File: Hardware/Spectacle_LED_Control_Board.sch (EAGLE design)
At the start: 44 parts, among them J3 USB-MICROB, J4 AUDIO-JACK3, J8 AUDIO-JACK3, U1 CY8C4146LQI-S422, U2 3.3V/150mA, U4 SN74LVC1G66, U5 SN74LVC1G66

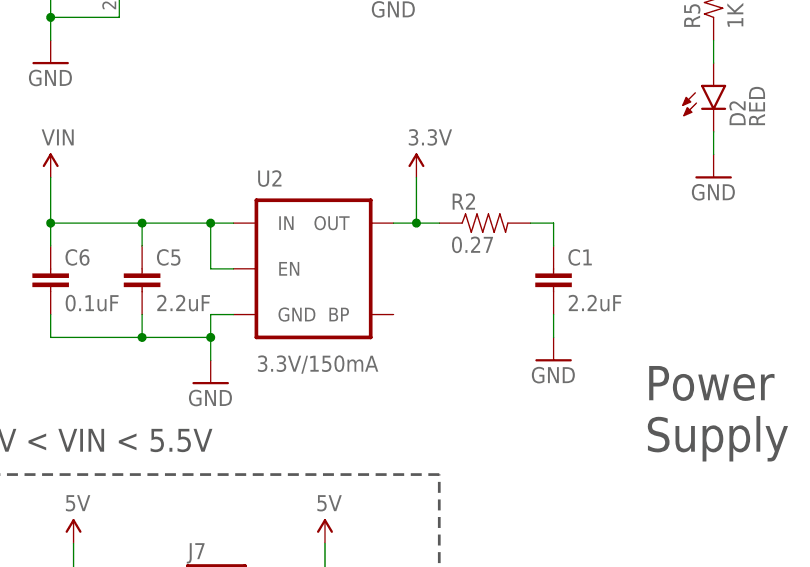
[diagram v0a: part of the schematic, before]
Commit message: Chg VREG to APK2112
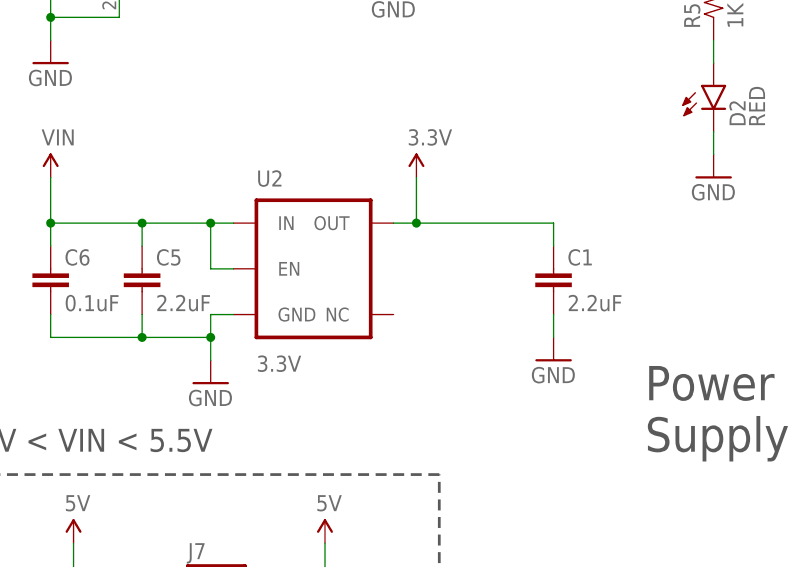
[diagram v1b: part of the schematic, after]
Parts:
- removed R2: 0.27, SparkFun-Resistors:0.27OHM-1/10W-1%(0603)
- U2: value 3.3V/150mA -> 3.3V; device SparkFun-PowerIC:V_REG_MIC52053.3V -> SparkFun-PowerIC:V_REG_AP2112K-3.3V
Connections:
- removed net N$3: C1.1, R2.2
- net 3.3V: now also C1.1; no longer R2.1
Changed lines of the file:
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@@
 <part name="GND1" library="SparkFun-Aesthetics" deviceset="GND" device=""/>
 <part name="SUPPLY2" library="SparkFun-Aesthetics" deviceset="VIN" device=""/>
-<part name="U2" library="SparkFun-PowerIC" deviceset="V_REG_MIC5205" device="3.3V" value="3.3V/150mA"/>
+<part name="U2" library="SparkFun-PowerIC" deviceset="V_REG_AP2112" device="K-3.3V" value="3.3V"/>
 <part name="GND6" library="SparkFun-Aesthetics" deviceset="GND" device=""/>
 <part name="SUPPLY3" library="SparkFun-Aesthetics" deviceset="VCC" device=""/>
 <part name="R1" library="SparkFun-Resistors" deviceset="10KOHM-1/10W-1%(0603)" device="0603" value="10K"/>
 <part name="GND7" library="SparkFun-Aesthetics" deviceset="GND" device=""/>
-<part name="R2" library="SparkFun-Resistors" deviceset="0.27OHM-1/10W-1%(0603)" device="" value="0.27"/>
 <part name="C1" library="SparkFun-Capacitors" deviceset="2.2UF-10V-20%(0603)" device="" value="2.2uF"/>
 <part name="C2" library="SparkFun-Capacitors" deviceset="1.0UF-16V-10%(0402)" device="" value="1.0uF"/>
@@
 <instance part="GND1" gate="1" x="33.02" y="96.52"/>
 <instance part="SUPPLY2" gate="G$1" x="15.24" y="119.38"/>
-<instance part="U2" gate="U1" x="45.72" y="109.22"/>
+<instance part="U2" gate="G$1" x="45.72" y="109.22"/>
 <instance part="GND6" gate="1" x="15.24" y="132.08"/>
 <instance part="SUPPLY3" gate="G$1" x="17.78" y="175.26"/>
 <instance part="R1" gate="G$1" x="35.56" y="165.1" rot="R90"/>
 <instance part="GND7" gate="1" x="71.12" y="99.06"/>
-<instance part="R2" gate="G$1" x="63.5" y="114.3"/>
 <instance part="C1" gate="G$1" x="71.12" y="106.68"/>
 <instance part="C2" gate="G$1" x="71.12" y="167.64"/>
@@
 </segment>
 <segment>
-<pinref part="U2" gate="U1" pin="GND"/>
+<pinref part="U2" gate="G$1" pin="GND"/>
 <pinref part="GND1" gate="1" pin="GND"/>
 <wire x1="35.56" y1="104.14" x2="33.02" y2="104.14" width="0.1524" layer="91"/>
@@
 </segment>
 </net>
-<net name="N$3" class="0">
-<segment>
-<pinref part="R2" gate="G$1" pin="2"/>
-<wire x1="68.58" y1="114.3" x2="71.12" y2="114.3" width="0.1524" layer="91"/>
-<pinref part="C1" gate="G$1" pin="1"/>
-<wire x1="71.12" y1="114.3" x2="71.12" y2="111.76" width="0.1524" layer="91"/>
-</segment>
-</net>
 <net name="VIN" class="0">
 <segment>
-<pinref part="U2" gate="U1" pin="EN"/>
+<pinref part="U2" gate="G$1" pin="EN"/>
 <wire x1="35.56" y1="109.22" x2="33.02" y2="109.22" width="0.1524" layer="91"/>
 <wire x1="33.02" y1="109.22" x2="33.02" y2="114.3" width="0.1524" layer="91"/>
-<pinref part="U2" gate="U1" pin="IN"/>
+<pinref part="U2" gate="G$1" pin="IN"/>
 <wire x1="35.56" y1="114.3" x2="33.02" y2="114.3" width="0.1524" layer="91"/>
 <junction x="33.02" y="114.3"/>
@@
 </segment>
 <segment>
-<pinref part="U2" gate="U1" pin="OUT"/>
+<pinref part="U2" gate="G$1" pin="OUT"/>
 <wire x1="53.34" y1="114.3" x2="55.88" y2="114.3" width="0.1524" layer="91"/>
 <wire x1="55.88" y1="114.3" x2="55.88" y2="119.38" width="0.1524" layer="91"/>
-<pinref part="R2" gate="G$1" pin="1"/>
-<wire x1="55.88" y1="114.3" x2="58.42" y2="114.3" width="0.1524" layer="91"/>
 <junction x="55.88" y="114.3"/>
 <pinref part="SUPPLY9" gate="G$1" pin="3.3V"/>
-</segment>
-<segment>
+<pinref part="C1" gate="G$1" pin="1"/>
+<wire x1="71.12" y1="114.3" x2="71.12" y2="111.76" width="0.1524" layer="91"/>
+<wire x1="55.88" y1="114.3" x2="71.12" y2="114.3" width="0.1524" layer="91"/>
+</segment>
+<segment>

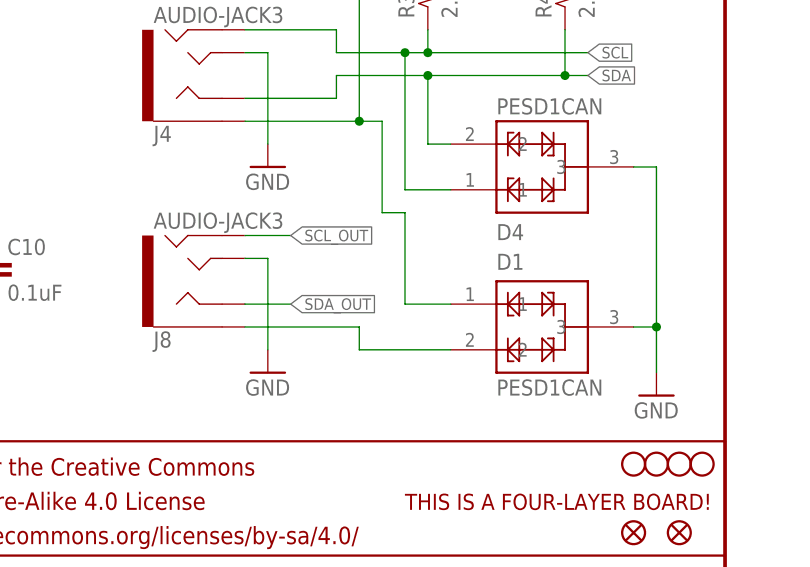
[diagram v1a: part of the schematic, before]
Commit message: Fix VIN path per review
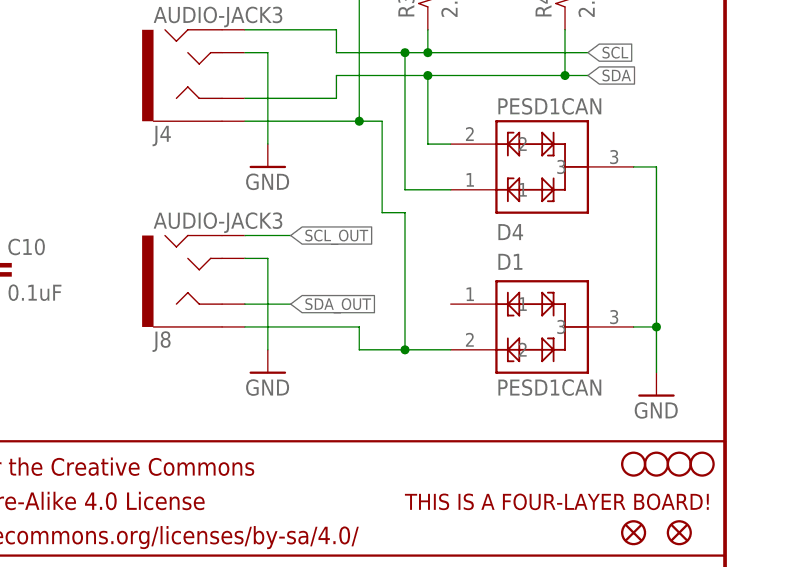
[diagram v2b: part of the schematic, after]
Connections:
- removed net N$1: D1.2, J8.EARTH
- net VIN: now also D1.2, J8.EARTH; no longer D1.1
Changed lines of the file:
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@@
 <wire x1="205.74" y1="91.44" x2="208.28" y2="91.44" width="0.1524" layer="91"/>
 <junction x="208.28" y="91.44"/>
-<pinref part="D1" gate="G$1" pin="1"/>
-<wire x1="218.44" y1="50.8" x2="213.36" y2="50.8" width="0.1524" layer="91"/>
-<wire x1="213.36" y1="50.8" x2="213.36" y2="60.96" width="0.1524" layer="91"/>
 <wire x1="213.36" y1="60.96" x2="210.82" y2="60.96" width="0.1524" layer="91"/>
 <wire x1="210.82" y1="60.96" x2="210.82" y2="71.12" width="0.1524" layer="91"/>
 <wire x1="210.82" y1="71.12" x2="208.28" y2="71.12" width="0.1524" layer="91"/>
 <junction x="208.28" y="71.12"/>
+<pinref part="D1" gate="G$1" pin="2"/>
+<pinref part="J8" gate="G$1" pin="EARTH"/>
+<wire x1="195.58" y1="48.26" x2="208.28" y2="48.26" width="0.1524" layer="91"/>
+<wire x1="208.28" y1="45.72" x2="208.28" y2="48.26" width="0.1524" layer="91"/>
+<wire x1="208.28" y1="45.72" x2="213.36" y2="45.72" width="0.1524" layer="91"/>
+<wire x1="213.36" y1="45.72" x2="218.44" y2="45.72" width="0.1524" layer="91"/>
+<wire x1="213.36" y1="60.96" x2="213.36" y2="45.72" width="0.1524" layer="91"/>
+<junction x="213.36" y="45.72"/>
 </segment>
 <segment>
@@
 </segment>
 </net>
-<net name="N$1" class="0">
-<segment>
-<pinref part="D1" gate="G$1" pin="2"/>
-<pinref part="J8" gate="G$1" pin="EARTH"/>
-<wire x1="195.58" y1="48.26" x2="208.28" y2="48.26" width="0.1524" layer="91"/>
-<wire x1="208.28" y1="45.72" x2="208.28" y2="48.26" width="0.1524" layer="91"/>
-<wire x1="208.28" y1="45.72" x2="218.44" y2="45.72" width="0.1524" layer="91"/>
-</segment>
-</net>

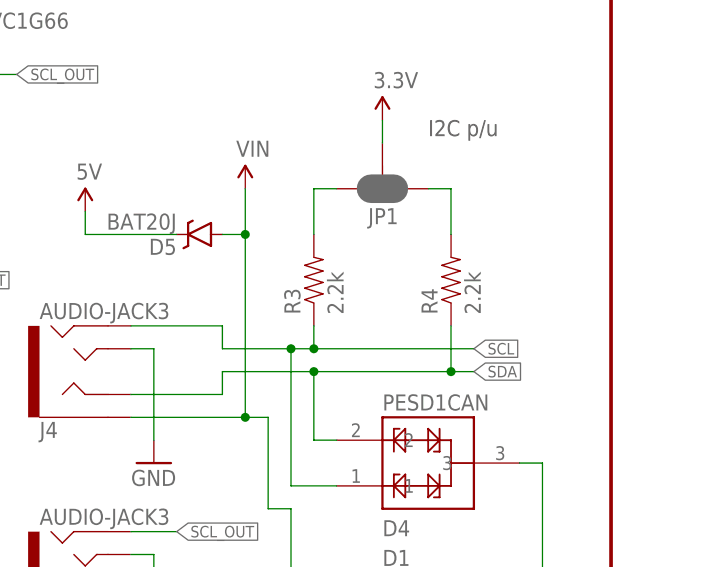
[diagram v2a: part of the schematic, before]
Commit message: Change pullups to 4.7k
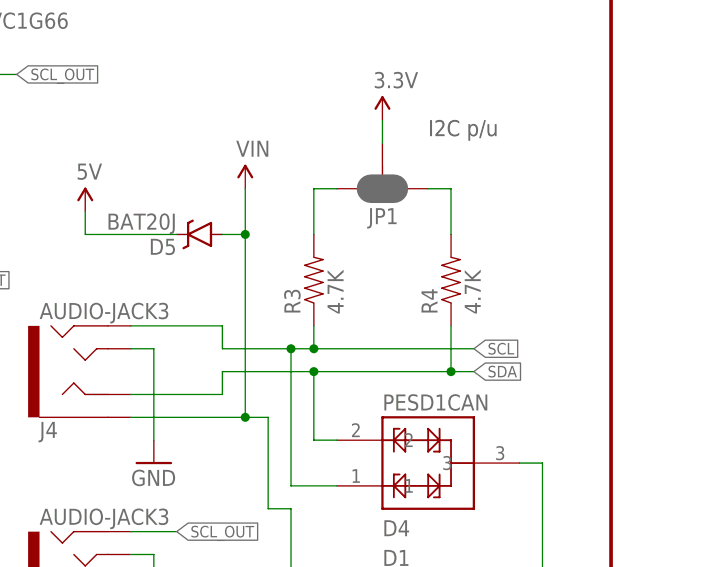
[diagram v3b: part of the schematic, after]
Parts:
- R3, R4: value 2.2k -> 4.7K; device SparkFun-Resistors:2.2KOHM-1/10W-1%(0603) -> SparkFun-Resistors:4.7KOHM-1/10W-1%(0603)
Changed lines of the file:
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@@
 <part name="GND9" library="SparkFun-Aesthetics" deviceset="GND" device=""/>
 <part name="SUPPLY7" library="SparkFun-Aesthetics" deviceset="VIN" device=""/>
-<part name="R3" library="SparkFun-Resistors" deviceset="2.2KOHM-1/10W-1%(0603)" device="" value="2.2k"/>
-<part name="R4" library="SparkFun-Resistors" deviceset="2.2KOHM-1/10W-1%(0603)" device="" value="2.2k"/>
+<part name="R3" library="SparkFun-Resistors" deviceset="4.7KOHM-1/10W-1%(0603)" device="" value="4.7K"/>
+<part name="R4" library="SparkFun-Resistors" deviceset="4.7KOHM-1/10W-1%(0603)" device="" value="4.7K"/>
 <part name="JP1" library="SparkFun-Passives" deviceset="JUMPER-PAD-3-NC_BY_PASTE" device=""/>
 <part name="J2" library="SparkFun-Connectors" deviceset="M05" device="NO_SILK"/>

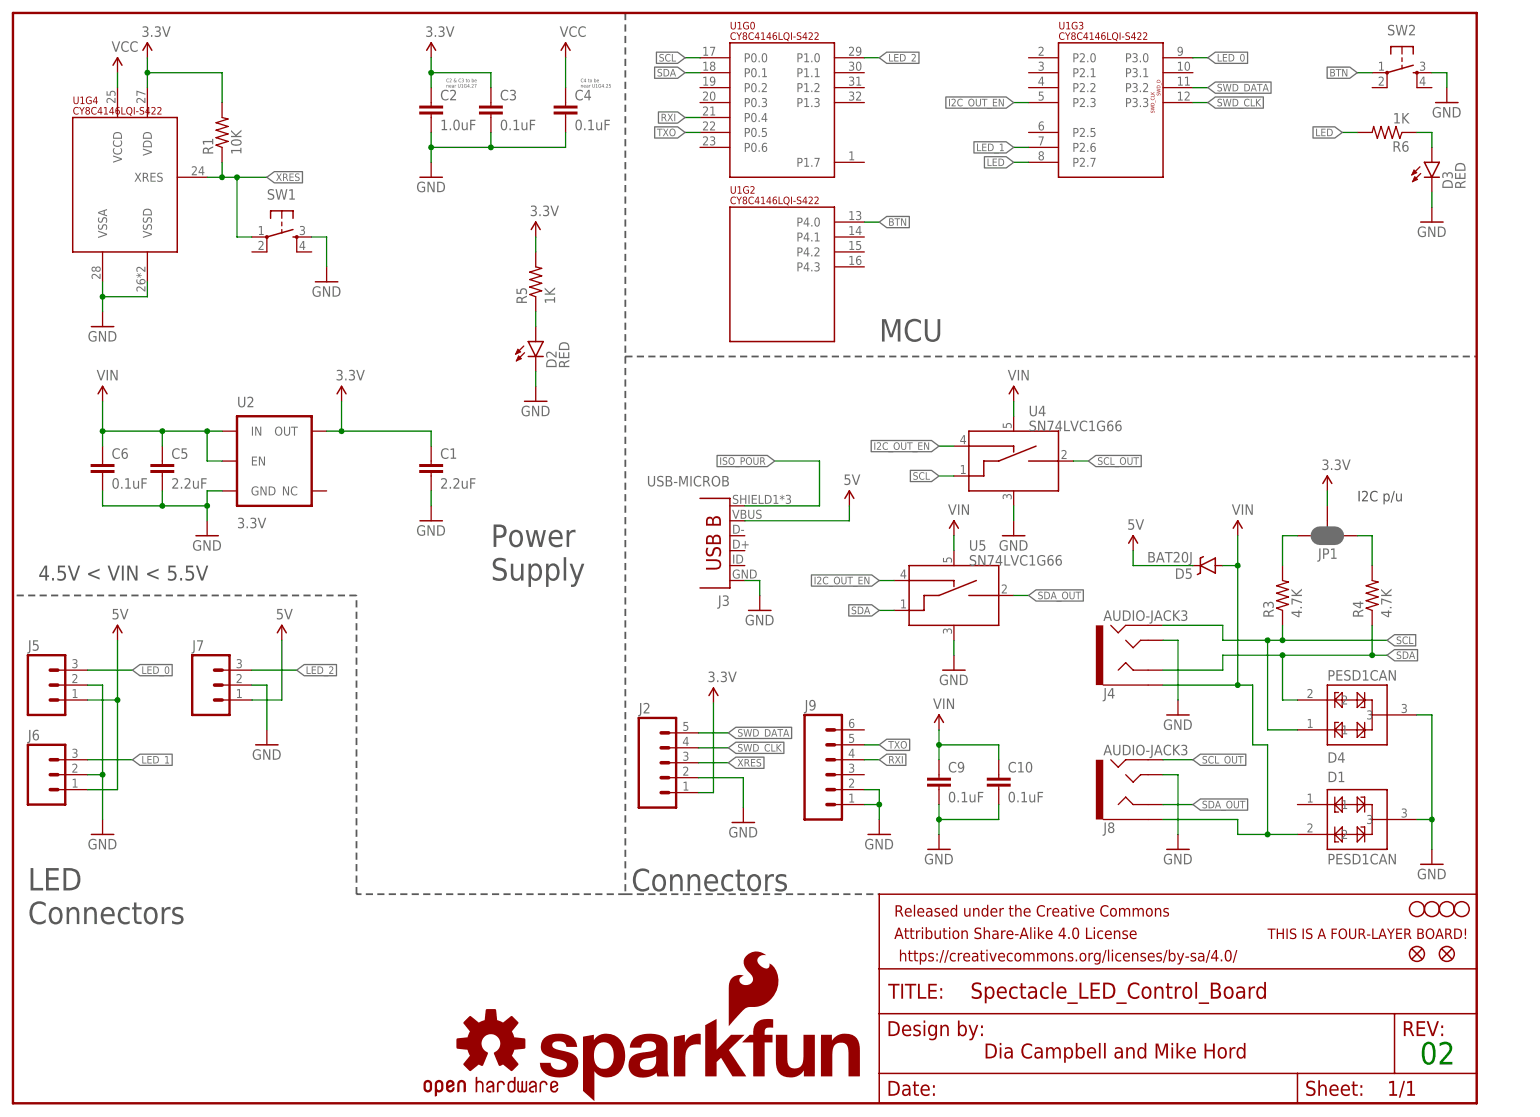
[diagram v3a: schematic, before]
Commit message: Primarily for changing to PSOC4245LQI-483 Interstitial commit for firmware
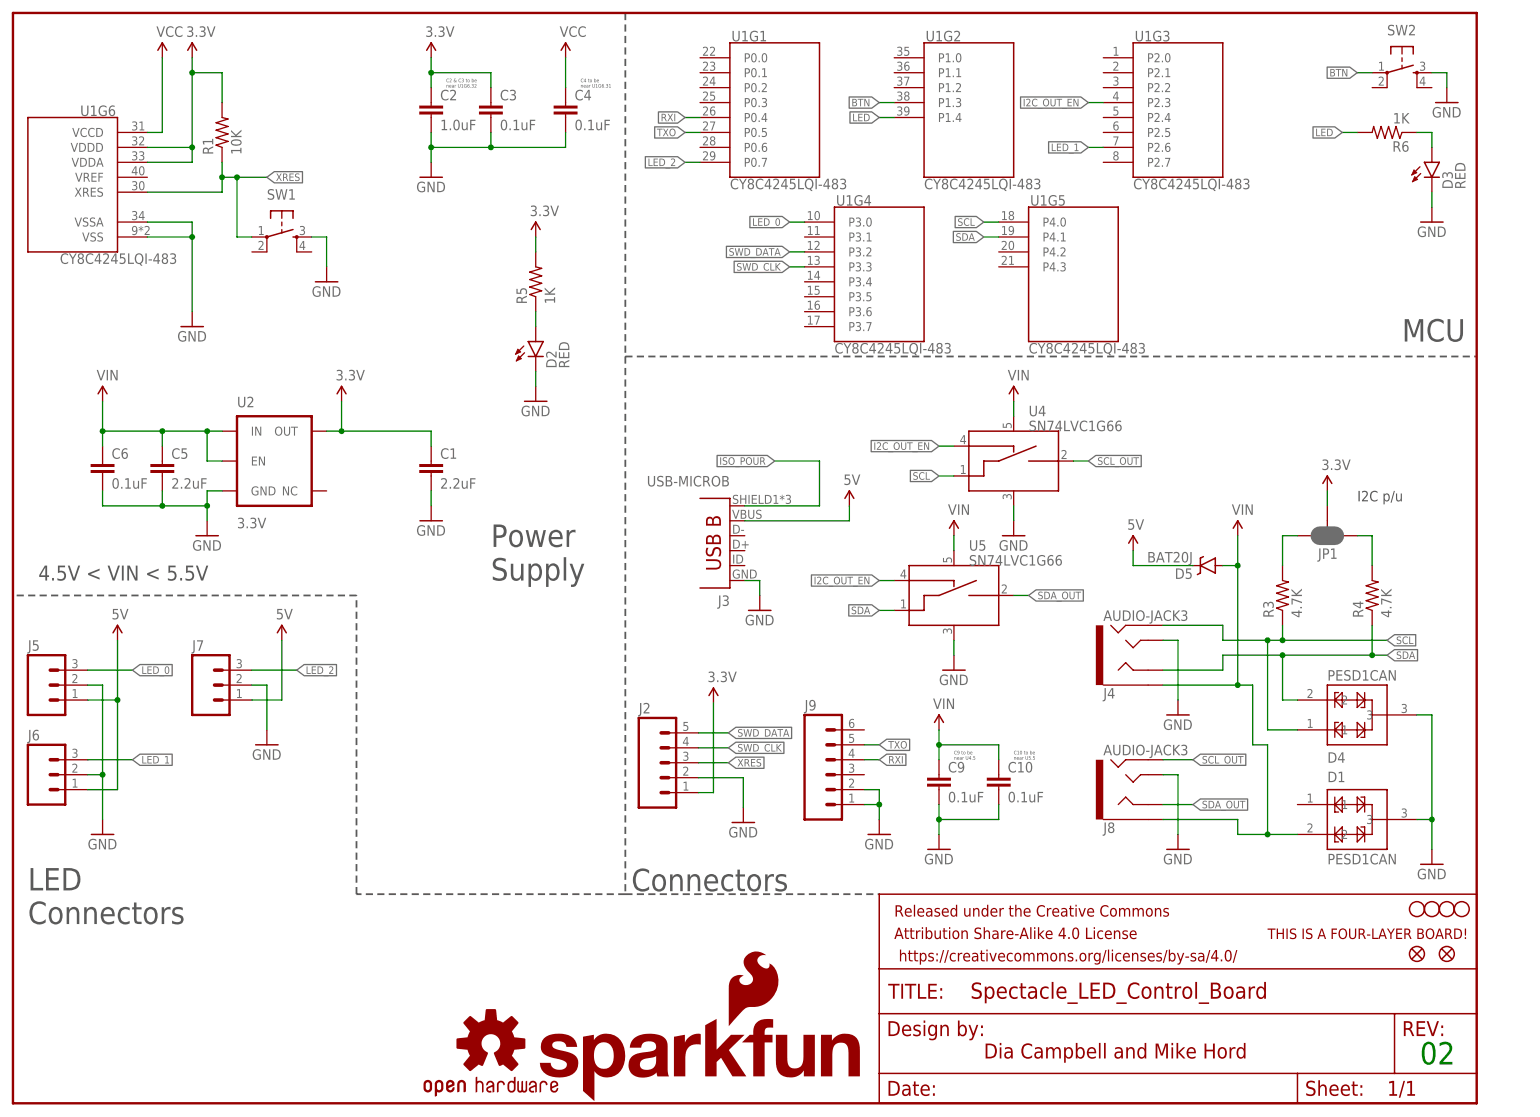
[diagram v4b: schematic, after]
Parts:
- U1: value CY8C4146LQI-S422 -> CY8C4245LQI-483; device SparkFun-DigitalIC:PSOC4_4100S_32QFN -> SparkFun-IC-Microcontroller:PSOC4_4200_40QFN
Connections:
- net 3.3V: now also U1G6.VDDA, U1G6.VDDD; no longer U1G4.VDD
- net BTN: now also U1G2.P1.3; no longer U1G2.P4.0
- net GND: now also U1G6.VSS, U1G6.VSSA; no longer U1G4.VSSA, U1G4.VSSD
- net LED: now also U1G2.P1.4; no longer U1G3.P2.7
- net LED_0: now also U1G4.P3.0; no longer U1G3.P3.0
- net LED_2: now also U1G1.P0.7; no longer U1G0.P1.0
- net RXI: now also U1G1.P0.4; no longer U1G0.P0.4
- net SCL: now also U1G5.P4.0; no longer U1G0.P0.0
- net SDA: now also U1G5.P4.1; no longer U1G0.P0.1
- net SWD_CLK: now also U1G4.P3.3; no longer U1G3.P3.3
- net SWD_DATA: now also U1G4.P3.2; no longer U1G3.P3.2
- net TXO: now also U1G1.P0.5; no longer U1G0.P0.5
- net VCC: now also U1G6.VCCD; no longer U1G4.VCCD
- net XRES: now also U1G6.XRES; no longer U1G4.XRES
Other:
- note added: "C10 to be near U5.5"
- note added: "C2 & C3 to be near U1G6.32"
- note added: "C4 to be near U1G6.31"
- note added: "C9 to be near U4.5"
- note removed: "C2 & C3 to be near U1G4.27"
- note removed: "C4 to be near U1G4.25"

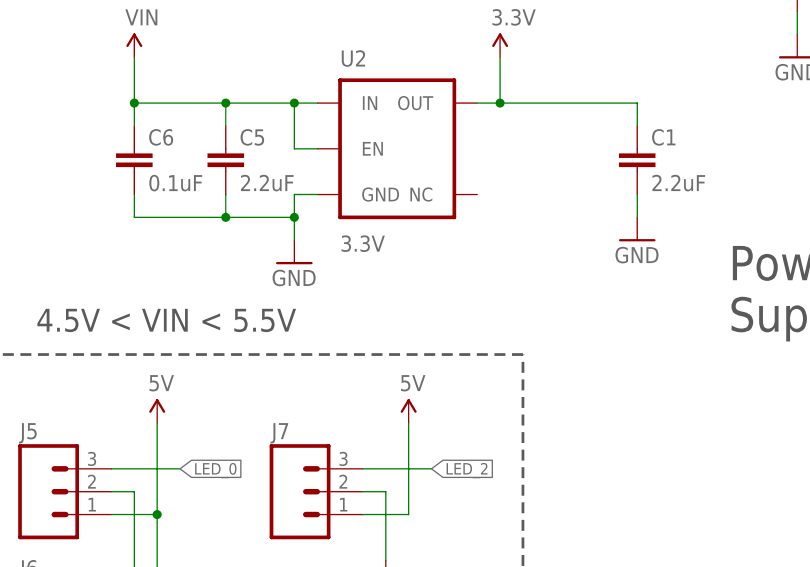
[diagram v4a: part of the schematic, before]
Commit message: moving caps
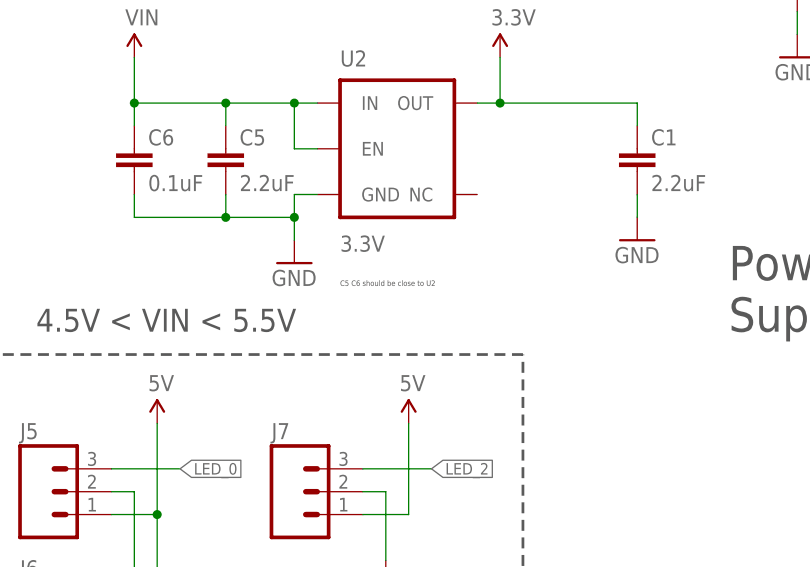
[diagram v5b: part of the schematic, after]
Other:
- note added: "C5 C6 should be close to U2"
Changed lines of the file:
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@@
 <?xml version="1.0" encoding="utf-8"?>
 <!DOCTYPE eagle SYSTEM "eagle.dtd">
-<eagle version="7.7.0">
+<eagle version="7.6.0">
 <drawing>
 <settings>
@@
 <text x="170.18" y="58.42" size="0.6096" layer="97">C10 to be
 near U5.5</text>
+<text x="38.1" y="93.98" size="0.6096" layer="97">C5 C6 should be close to U2</text>
 </plain>
 <instances>
